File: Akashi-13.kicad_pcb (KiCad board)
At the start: 2 copper layers, 67.3 x 91.4 mm, 28 parts, among them J1 Conn_02x35_Odd_Even, J2 Conn_02x35_Odd_Even, J3 J0011D01BNL, U1 LAN9220-ABZJ, U2 93AA46AT-IOT, X1 DFA-S15

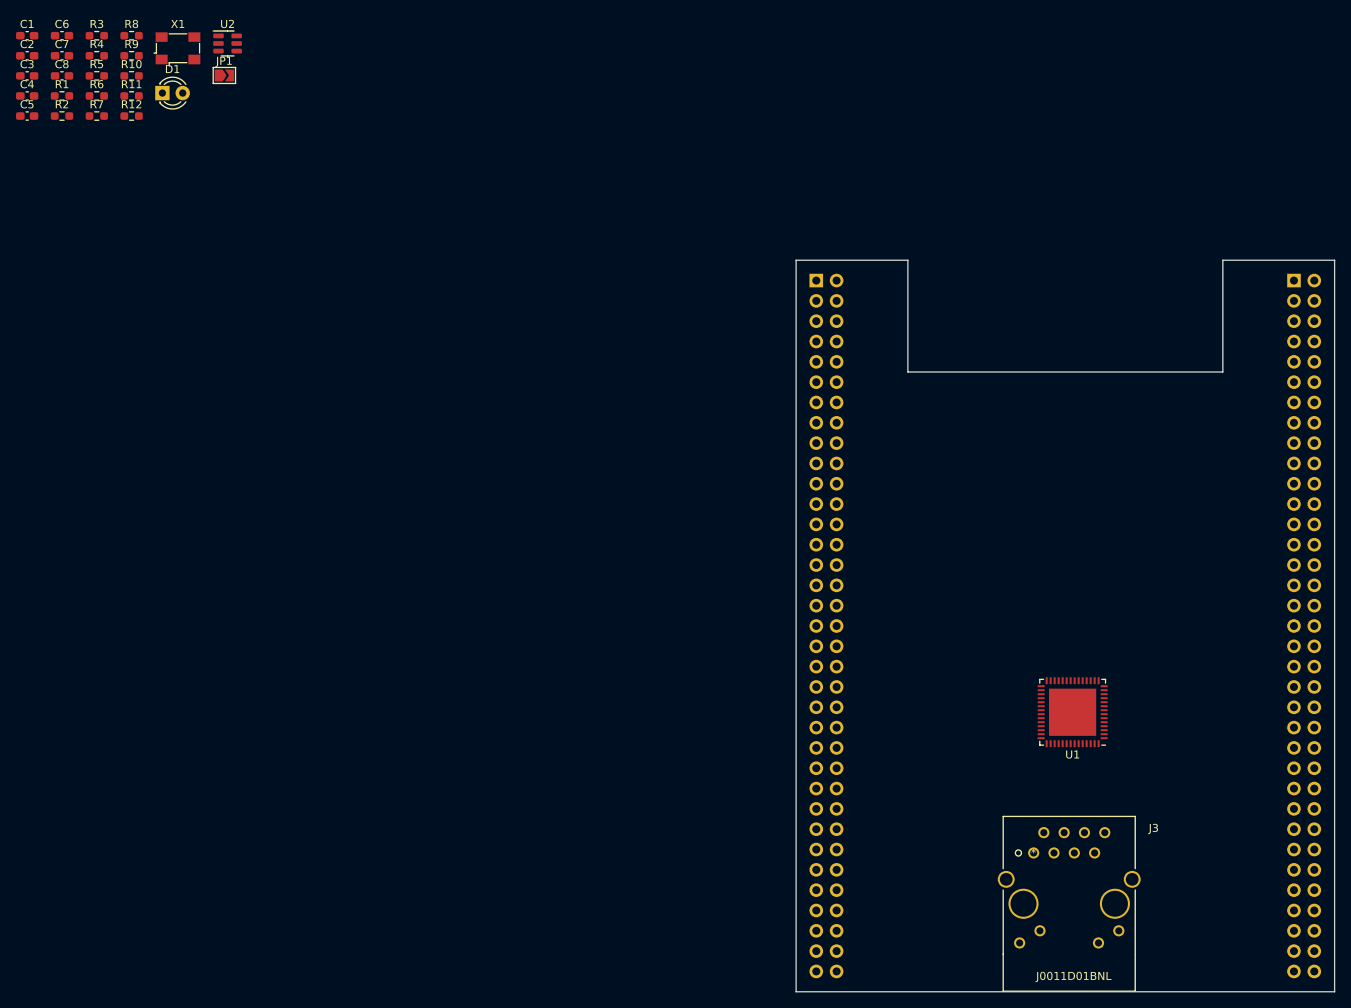
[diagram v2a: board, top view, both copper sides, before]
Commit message: Finished to input schematics.
ERC OK.
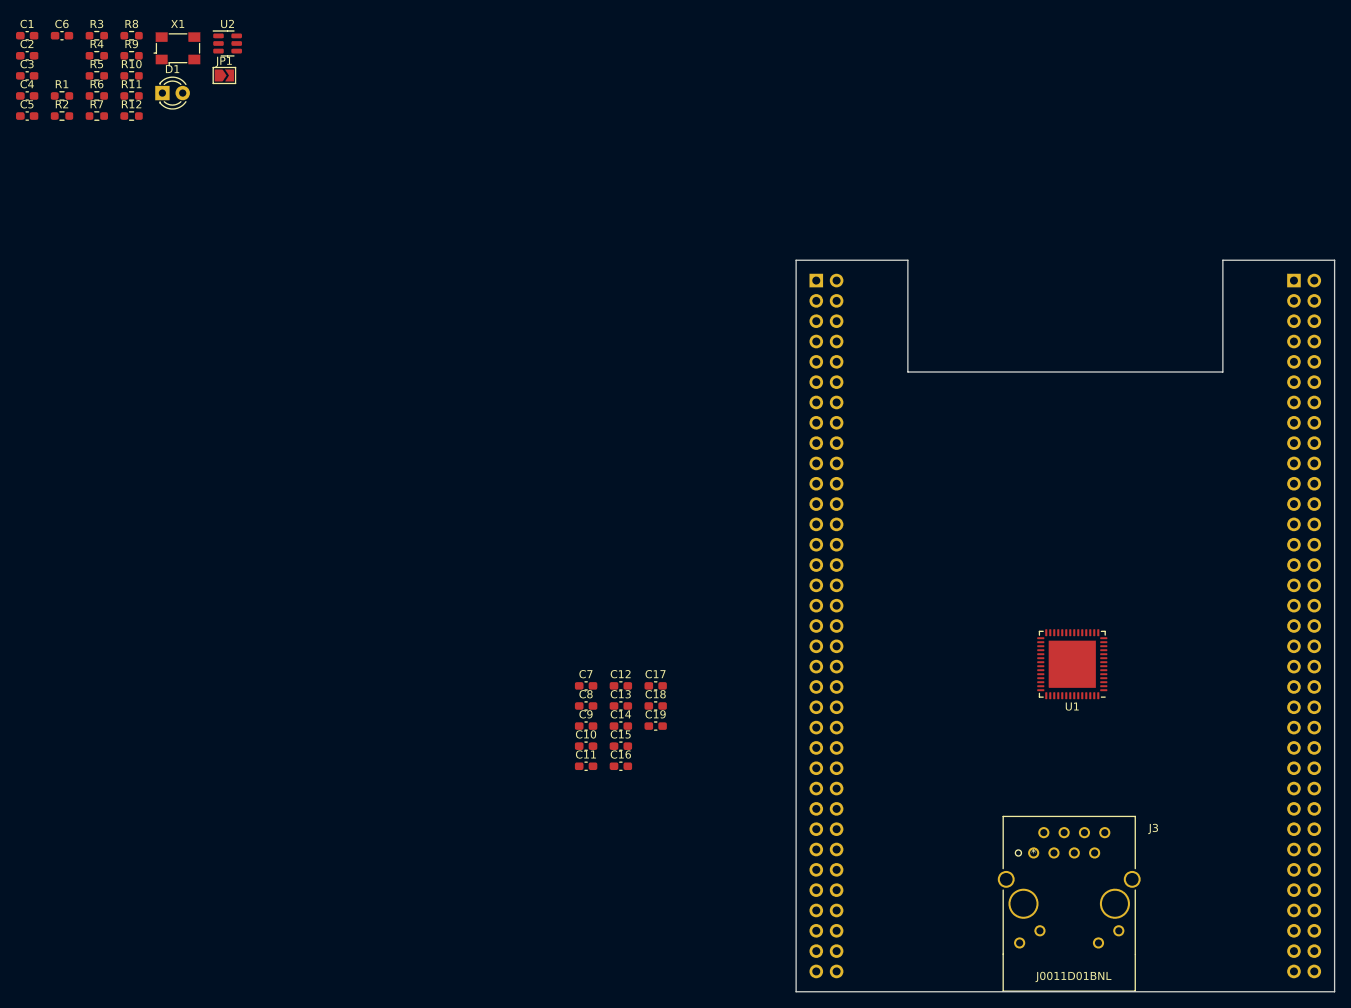
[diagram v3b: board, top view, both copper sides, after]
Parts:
- added C10: 0.1u, Capacitor_SMD:C_0603_1608Metric_Pad1.08x0.95mm_HandSolder, F.Cu at (71.5, 124.2)
- added C11: 4.7u, Capacitor_SMD:C_0603_1608Metric_Pad1.08x0.95mm_HandSolder, F.Cu at (71.5, 126.8)
- added C12: 0.1u, Capacitor_SMD:C_0603_1608Metric_Pad1.08x0.95mm_HandSolder, F.Cu at (75.9, 116.7)
- added C13: 10u, Capacitor_SMD:C_0603_1608Metric_Pad1.08x0.95mm_HandSolder, F.Cu at (75.9, 119.2)
- added C14: 0.1u, Capacitor_SMD:C_0603_1608Metric_Pad1.08x0.95mm_HandSolder, F.Cu at (75.9, 121.7)
- added C15: 0.1u, Capacitor_SMD:C_0603_1608Metric_Pad1.08x0.95mm_HandSolder, F.Cu at (75.9, 124.2)
- added C16: 0.1u, Capacitor_SMD:C_0603_1608Metric_Pad1.08x0.95mm_HandSolder, F.Cu at (75.9, 126.8)
- added C17: 0.1u, Capacitor_SMD:C_0603_1608Metric_Pad1.08x0.95mm_HandSolder, F.Cu at (80.2, 116.7)
- added C18: 0.1u, Capacitor_SMD:C_0603_1608Metric_Pad1.08x0.95mm_HandSolder, F.Cu at (80.2, 119.2)
- added C19: 0.022u, Capacitor_SMD:C_0603_1608Metric_Pad1.08x0.95mm_HandSolder, F.Cu at (80.2, 121.7)
- added C9: 10u, Capacitor_SMD:C_0603_1608Metric_Pad1.08x0.95mm_HandSolder, F.Cu at (71.5, 121.7)
- C1, C2, C3, C4: value C_Small -> 15p
- C5, C6, C8: value C_Small -> 0.1u
- C7: value C_Small -> 4.7u
- R1, R12, R2: value R -> 300
- R10, R8: value R -> 10k
- R11: value R -> 12.4k
- R3: value R -> 10
- R4, R5, R6, R7: value R -> 50
- R9: value R -> 4.7k
- moved C7 102.4 mm to (71.5, 116.7)
- moved C8 102.4 mm to (71.5, 119.2)
- moved U1 6.00 mm to (132.3, 114.0)
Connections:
- J1 pad 53: /A0 -> unconnected-(J1-Pin_53-Pad53)
- J3 pad 4: GND -> Net-(C19-Pad1)
- J3 pad 5: GND -> Net-(C19-Pad1)
- R10 pad 1: /EPP_CS -> /EEP_CS
- R3 pad 2: GND -> Net-(C19-Pad1)
- U2 pad 5: /EPP_CS -> /EEP_CS

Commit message: All bypass chapacitor of LAN9220 and XTAL are placed.
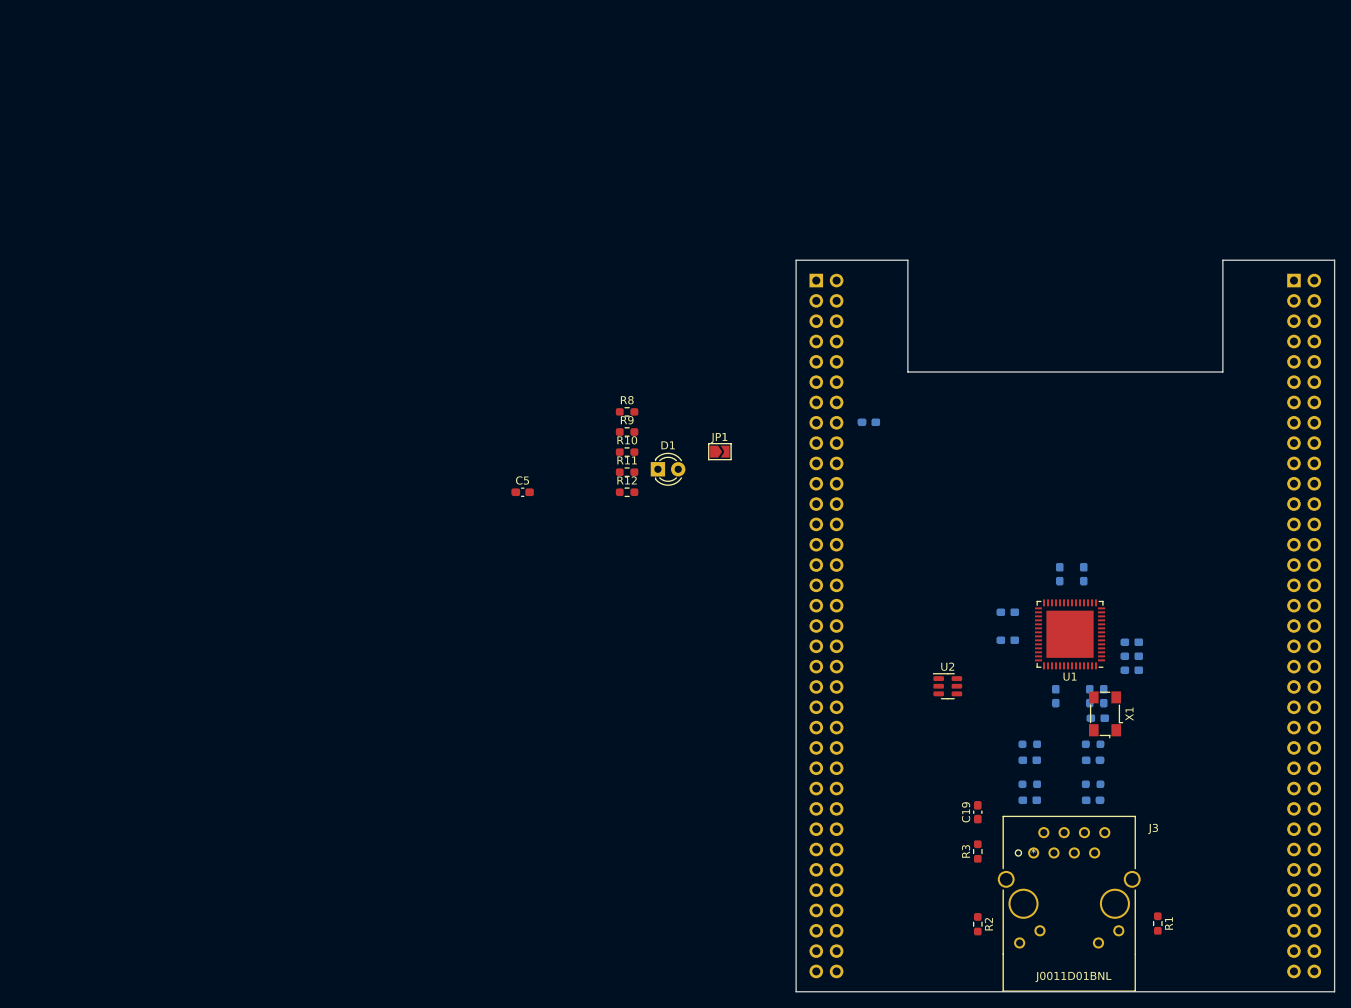
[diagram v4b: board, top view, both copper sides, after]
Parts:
- removed C18: 0.1u, Capacitor_SMD:C_0603_1608Metric_Pad1.08x0.95mm_HandSolder
- C1, C10, C11, C12, C2, C3, C4, C6, C7, C8, C9, R4, R5, R6, R7: moved to B.Cu
- C13: value 10u -> 0.1u; moved to B.Cu
- C14, C15, C16, C17: value 0.1u -> 4.7u; moved to B.Cu
- moved R1 171.6 mm to (143.0, 146.4), turned to -90 degrees
- moved C1 161.1 mm to (134.9, 126.0)
- moved C3 161.1 mm to (134.9, 131.0)
- moved C6 155.1 mm to (135.5, 120.8)
- moved C2 153.2 mm to (127.0, 126.0), turned to 180 degrees
- moved C4 153.2 mm to (127.0, 131.0), turned to 180 degrees
- moved R2 152.7 mm to (120.5, 146.5), turned to -90 degrees
- moved R4 151.4 mm to (134.9, 124.0), turned to 180 degrees
- moved R6 151.4 mm to (134.9, 129.0), turned to 180 degrees
- moved R3 150.1 mm to (120.5, 137.4), turned to 90 degrees
- moved R5 143.5 mm to (127.0, 124.0)
- moved R7 143.4 mm to (127.0, 129.0)
- moved X1 142.6 mm to (136.4, 120.2), turned to 90 degrees
- moved U2 120.7 mm to (116.8, 116.8)
- moved C5 77.8 mm to (63.6, 92.5)
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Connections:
- C11 pad 2: Net-(C11-Pad2) -> GND
- C12 pad 2: Net-(C11-Pad2) -> GND
- C13 pad 2: Net-(C11-Pad2) -> GND
- C14 pad 2: Net-(C11-Pad2) -> GND

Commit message: Placed all parts
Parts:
- R11: moved to B.Cu
- moved R12 95.0 mm to (154.9, 146.4), turned to -90 degrees
- moved D1 88.6 mm to (149.9, 144.8), turned to -90 degrees
- moved R11 62.5 mm to (132.5, 118.0), turned to -90 degrees
- moved C5 56.4 mm to (115.9, 113.8), turned to 180 degrees
- moved R9 54.8 mm to (118.0, 120.9), turned to 90 degrees
- moved R10 53.5 mm to (120.8, 117.8), turned to -90 degrees
- moved R8 49.6 mm to (112.5, 116.8), turned to -90 degrees
- moved JP1 49.5 mm to (127.2, 118.0), turned to -90 degrees
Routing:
- net +1V8: track 0.00 -> 20.6 mm, vias 0 -> 3
- net +3.3V: track 0.00 -> 12.0 mm, vias 0 -> 7
- net Net-(U1-EXRES): track 0.00 -> 1.89 mm, vias 0 -> 1
- net /TD+: track 0.00 -> 1.84 mm, vias 0 -> 1
- net /RD-: track 0.00 -> 1.80 mm, vias 0 -> 1
- net Net-(U1-XTAL1/CLKIN): track 0.00 -> 1.64 mm, vias 0 -> 1
- net /RD+: track 0.00 -> 1.30 mm, vias 0 -> 1
- net /TD-: track 0.00 -> 1.29 mm, vias 0 -> 1

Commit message: Fixed wrong courtyard of the J3.
Ready to autoroute.
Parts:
- J3: value J0011D01BNL -> CONN12_011D01BNL_PUL
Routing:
- added copper zone on F.Cu, net +3.3V
- added copper zone on B.Cu, net GND
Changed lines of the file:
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@@
         (effects (font (size 1 1) (thickness 0.15)))
     )
-    (fp_text value "J0011D01BNL" (at -5.017 -15.41) (layer "F.SilkS")
+    (fp_text value "CONN12_011D01BNL_PUL" (at -5.017 -15.41) (layer "F.SilkS") hide
         (effects (font (size 1 1) (thickness 0.15)))
     )
@@
     (fp_line (start -13.628098 -4.6081) (end -13.628098 -1.9919)
       (stroke (width 0.05) (type solid)) (layer "F.CrtYd"))
-    (fp_line (start -13.628098 -4.6081) (end -13.628098 -1.9919)
-      (stroke (width 0.05) (type solid)) (layer "F.CrtYd"))
     (fp_line (start -13.628098 -1.9919) (end -12.827 -1.9919)
       (stroke (width 0.05) (type solid)) (layer "F.CrtYd"))
-    (fp_line (start -13.628098 -1.9919) (end -12.827 -1.9919)
-      (stroke (width 0.05) (type solid)) (layer "F.CrtYd"))
     (fp_line (start -12.827 -17.404) (end -12.827 -4.6081)
       (stroke (width 0.05) (type solid)) (layer "F.CrtYd"))
-    (fp_line (start -12.827 -17.404) (end -12.827 -4.6081)
-      (stroke (width 0.05) (type solid)) (layer "F.CrtYd"))
     (fp_line (start -12.827 -4.6081) (end -13.628098 -4.6081)
       (stroke (width 0.05) (type solid)) (layer "F.CrtYd"))
-    (fp_line (start -12.827 -4.6081) (end -13.628098 -4.6081)
-      (stroke (width 0.05) (type solid)) (layer "F.CrtYd"))
     (fp_line (start -12.827 -1.9919) (end -12.827 4.694)
       (stroke (width 0.05) (type solid)) (layer "F.CrtYd"))
-    (fp_line (start -12.827 -1.9919) (end -12.827 4.694)
-      (stroke (width 0.05) (type solid)) (layer "F.CrtYd"))
     (fp_line (start -12.827 4.694) (end 3.937 4.694)
       (stroke (width 0.05) (type solid)) (layer "F.CrtYd"))
-    (fp_line (start -12.827 4.694) (end 3.937 4.694)
-      (stroke (width 0.05) (type solid)) (layer "F.CrtYd"))
     (fp_line (start 3.937 -17.404) (end -12.827 -17.404)
       (stroke (width 0.05) (type solid)) (layer "F.CrtYd"))
-    (fp_line (start 3.937 -17.404) (end -12.827 -17.404)
-      (stroke (width 0.05) (type solid)) (layer "F.CrtYd"))
     (fp_line (start 3.937 -4.6081) (end 3.937 -17.404)
       (stroke (width 0.05) (type solid)) (layer "F.CrtYd"))
-    (fp_line (start 3.937 -4.6081) (end 3.937 -17.404)
-      (stroke (width 0.05) (type solid)) (layer "F.CrtYd"))
     (fp_line (start 3.937 -1.9919) (end 4.738098 -1.9919)
       (stroke (width 0.05) (type solid)) (layer "F.CrtYd"))
-    (fp_line (start 3.937 -1.9919) (end 4.738098 -1.9919)
-      (stroke (width 0.05) (type solid)) (layer "F.CrtYd"))
     (fp_line (start 3.937 4.694) (end 3.937 -1.9919)
       (stroke (width 0.05) (type solid)) (layer "F.CrtYd"))
-    (fp_line (start 3.937 4.694) (end 3.937 -1.9919)
-      (stroke (width 0.05) (type solid)) (layer "F.CrtYd"))
     (fp_line (start 4.738098 -4.6081) (end 3.937 -4.6081)
-      (stroke (width 0.05) (type solid)) (layer "F.CrtYd"))
-    (fp_line (start 4.738098 -4.6081) (end 3.937 -4.6081)
-      (stroke (width 0.05) (type solid)) (layer "F.CrtYd"))
-    (fp_line (start 4.738098 -1.9919) (end 4.738098 -4.6081)
       (stroke (width 0.05) (type solid)) (layer "F.CrtYd"))
     (fp_line (start 4.738098 -1.9919) (end 4.738098 -4.6081)
@@
     (property "ki_keywords" "connector")
     (attr through_hole)
-    (fp_text reference "J2" (at -1.27 2.77) (layer "B.SilkS")
+    (fp_text reference "J2" (at 3.175 0) (layer "B.SilkS")
         (effects (font (size 1 1) (thickness 0.15)) (justify mirror))
     )
@@
     (property "ki_keywords" "connector")
     (attr through_hole)
-    (fp_text reference "J1" (at -1.27 2.77) (layer "B.SilkS")
+    (fp_text reference "J1" (at -5.735 0) (layer "B.SilkS")
         (effects (font (size 1 1) (thickness 0.15)) (justify mirror))
     )
@@
   (segment (start 134.78 114.1975) (end 134.78 115.53) (width 0.25) (layer "F.Cu") (net 143))
   (via (at 135 115.75) (size 0.6) (drill 0.2) (layers "F.Cu" "B.Cu") (net 143))
+  (zone (net 129) (net_name "+3.3V") (layer "F.Cu") (hatch edge 0.5)
+    (connect_pads (clearance 0.5))
+    (min_thickness 0.25) (filled_areas_thickness no)
+    (fill yes (thermal_gap 0.5) (thermal_bridge_width 0.5))
+    (polygon
+      (pts
+        (xy 98.425 64.135)
+        (xy 111.125 64.135)
+        (xy 111.125 78.105)
+        (xy 151.765 78.105)
+        (xy 151.765 64.135)
+        (xy 164.465 64.135)
+        (xy 164.465 154.305)
+        (xy 98.425 154.305)
+      )
+    )
+  )
+  (zone (net 16) (net_name "GND") (layer "B.Cu") (hatch edge 0.5)
+    (priority 1)
+    (connect_pads (clearance 0.5))
+    (min_thickness 0.25) (filled_areas_thickness no)
+    (fill yes (thermal_gap 0.5) (thermal_bridge_width 0.5))
+    (polygon
+      (pts
+        (xy 98.425 64.135)
+        (xy 111.125 64.135)
+        (xy 111.125 78.105)
+        (xy 151.765 78.105)
+        (xy 151.765 64.135)
+        (xy 164.465 64.135)
+        (xy 164.465 154.305)
+        (xy 98.425 154.305)
+      )
+    )
+  )
 )
